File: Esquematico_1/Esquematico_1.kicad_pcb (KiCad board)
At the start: 2 copper layers, 84.5 x 148.5 mm, 83 parts, among them IC1 AP2112K-3.3TRG1, J7 USB_C_Receptacle_USB2.0_16P, U1 ICM-42688-P, U2 STM32F405RGTx, U3 Mag, U4 BMP388, U5 USBLC6-2SC6, U6 TPS54302DDCR

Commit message: Update PCB y JST
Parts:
- removed the XTAL1 at (109.9, 30.8)
- added H1: MountingHole, MountingHole:MountingHole_2.7mm_M2.5_Pad_Via, F.Cu at (88.1, 170.1)
- added H2: MountingHole, MountingHole:MountingHole_2.7mm_M2.5_Pad_Via, F.Cu at (88.1, 136.1)
- added H3: MountingHole, MountingHole:MountingHole_2.7mm_M2.5_Pad_Via, F.Cu at (54.0, 136.0)
- added H4: MountingHole, MountingHole:MountingHole_2.7mm_M2.5_Pad_Via, F.Cu at (53.9, 170.1)
- added J1: Screw_Terminal_01x04, Connector_JST:JST_SH_SM04B-SRSS-TB_1x04-1MP_P1.00mm_Horizontal, F.Cu at (129.0, 144.5)
- added J2: Screw_Terminal_01x03, Connector_JST:JST_SH_SM03B-SRSS-TB_1x03-1MP_P1.00mm_Horizontal, F.Cu at (129.0, 152.0)
- added J3: Screw_Terminal_01x06, Connector_JST:JST_SH_SM06B-SRSS-TB_1x06-1MP_P1.00mm_Horizontal, F.Cu at (128.5, 160.5)
- added J4: Screw_Terminal_01x08, Connector_JST:JST_SH_SM08B-SRSS-TB_1x08-1MP_P1.00mm_Horizontal, F.Cu at (121.0, 168.0)
- added J5: SWD, Connector_PinHeader_1.00mm:PinHeader_1x06_P1.00mm_Vertical_SMD_Pin1Left, F.Cu at (77.6, 78.5)
- moved CARD1 123.5 mm to (64.2, 164.7)
- moved U2 117.1 mm to (113.5, 152.5)
- moved U4 115.4 mm to (81.2, 169.8), turned to 0 degrees
- moved U1 114.1 mm to (77.6, 169.5), turned to 0 degrees
- moved LSE1 109.3 mm to (101.3, 146.5)
- moved C15 108.7 mm to (68.0, 138.0), turned to 180 degrees
- moved L1 107.3 mm to (74.3, 137.0)
- moved C16 106.4 mm to (80.5, 134.5)
- moved R10 106.2 mm to (59.5, 134.5)
- moved R9 106.2 mm to (64.0, 134.5)
- moved C17 105.8 mm to (81.0, 137.0)
- moved C12 104.7 mm to (75.5, 144.1)
- moved R12 104.7 mm to (80.5, 144.5)
- moved R13 104.7 mm to (80.5, 147.4)
- moved C14 104.3 mm to (63.5, 138.5), turned to 90 degrees
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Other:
- board size 84.5 x 148.5 mm -> 84.5 x 148 mm

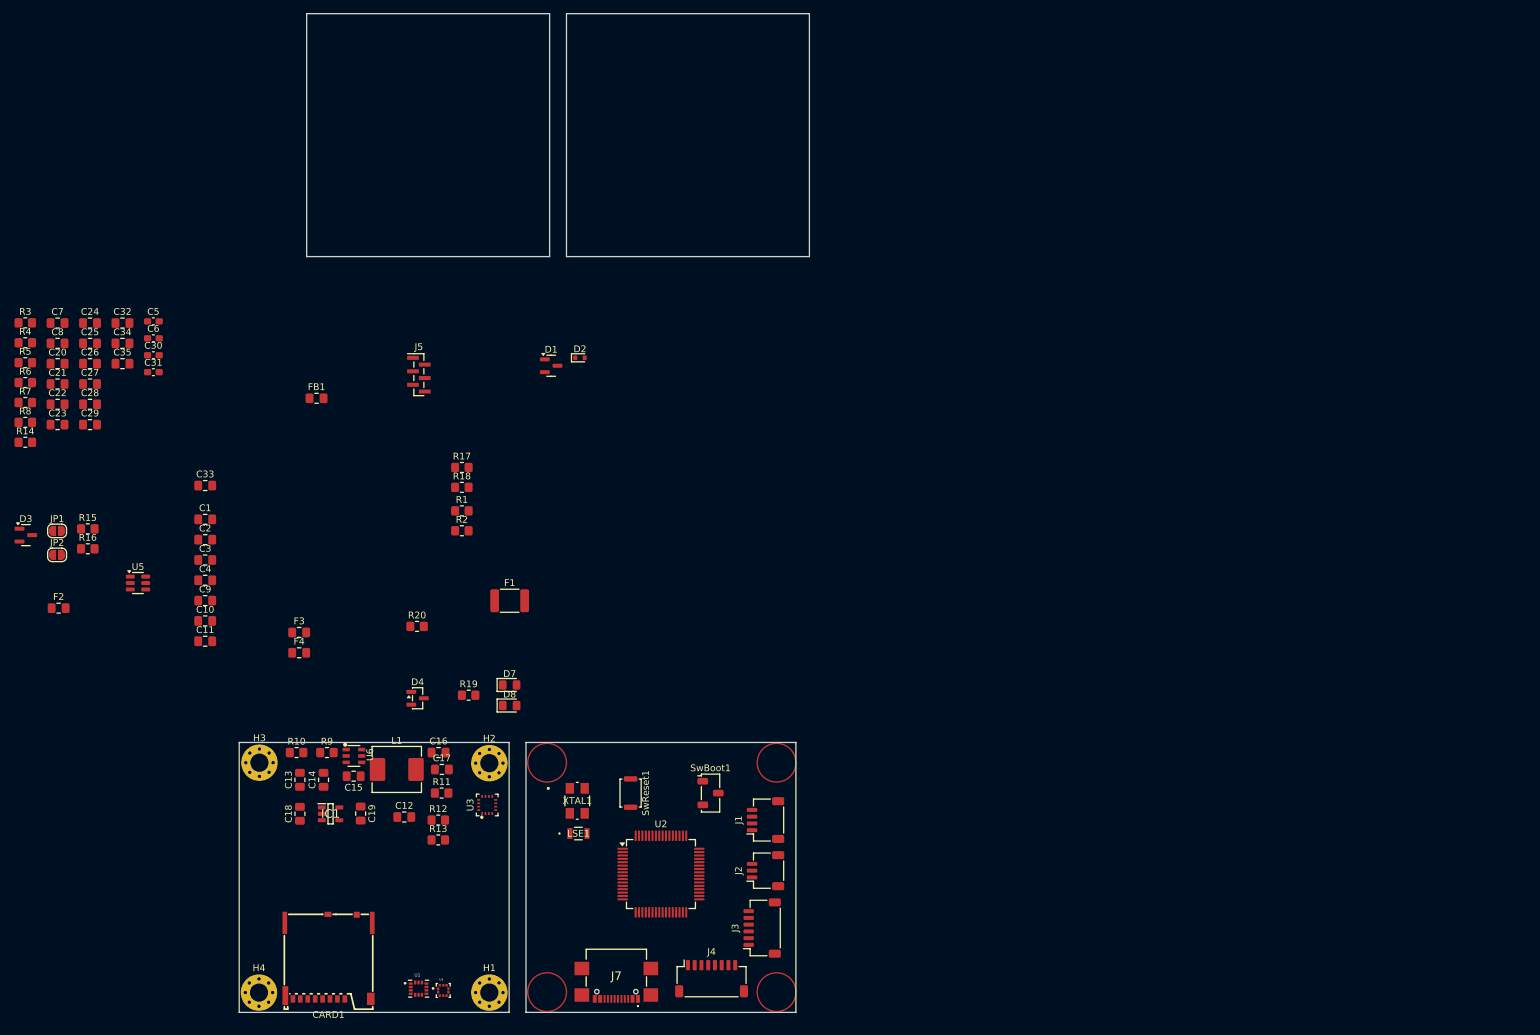
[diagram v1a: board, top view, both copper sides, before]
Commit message: Cambios netclasses, rules en el PCB, conección de los cristales
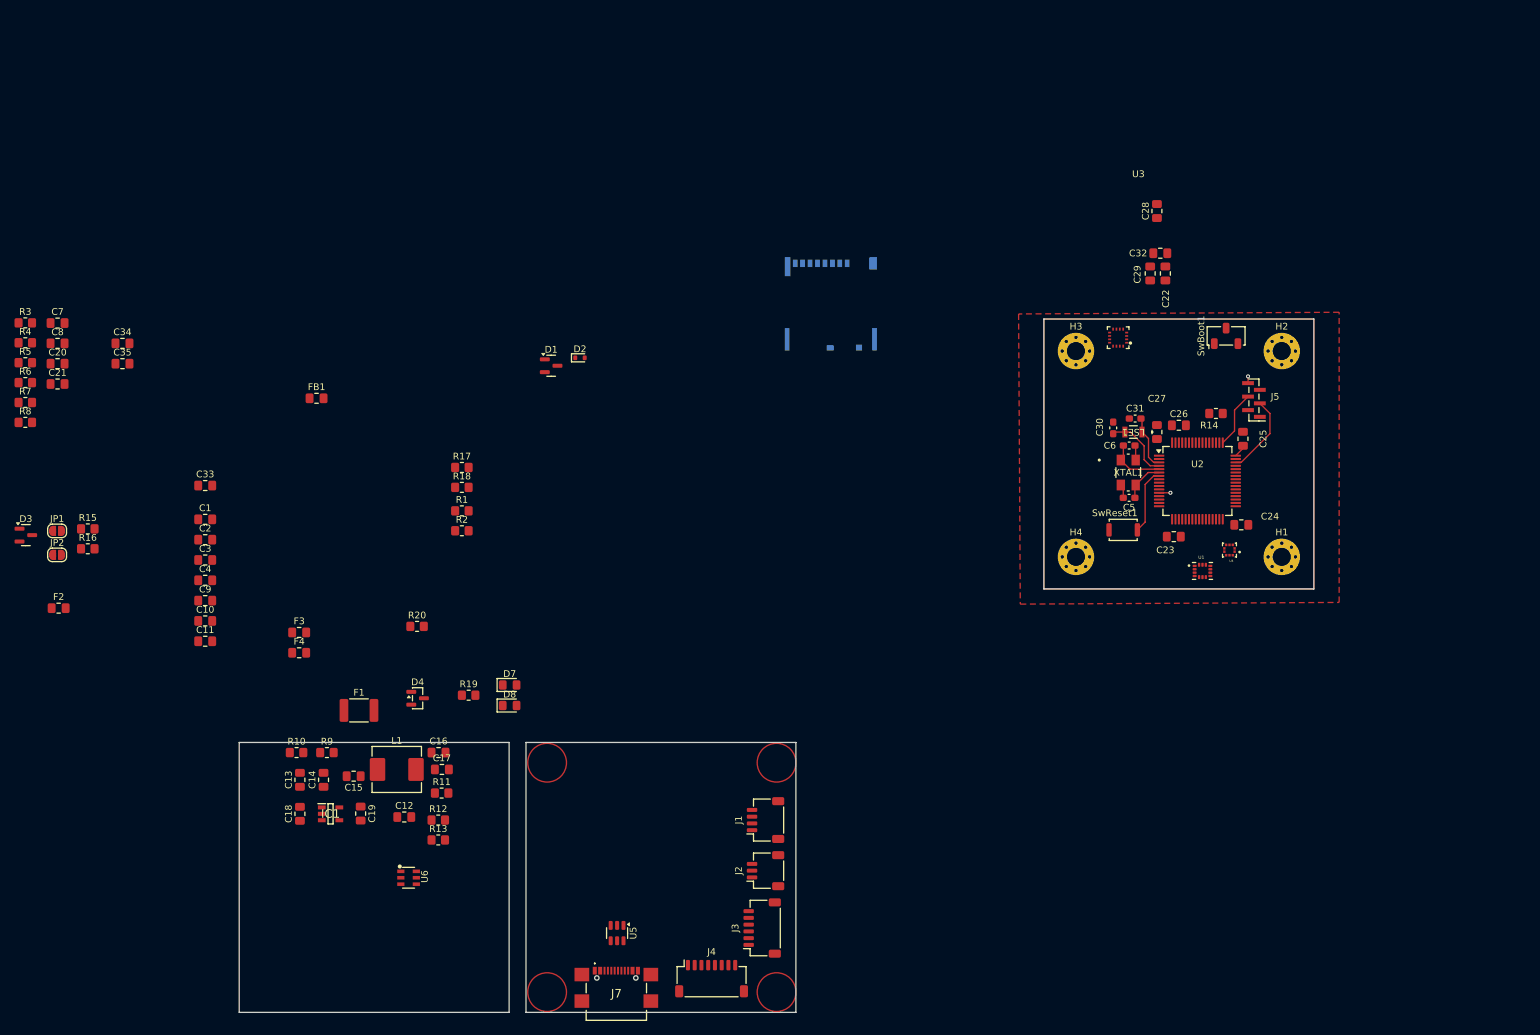
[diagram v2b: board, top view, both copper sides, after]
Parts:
- CARD1: moved to B.Cu
- moved R14 176.5 mm to (195.8, 84.2), turned to 180 degrees
- moved C24 173.2 mm to (199.5, 100.8)
- moved C25 171.4 mm to (199.8, 88.0), turned to 90 degrees
- moved C23 166.2 mm to (189.5, 102.5), turned to 180 degrees
- moved C22 165.3 mm to (188.2, 63.5), turned to 90 degrees
- moved C26 161.6 mm to (190.2, 86.0)
- moved C28 160.7 mm to (187.0, 54.2), turned to 90 degrees
- moved C29 158.7 mm to (186.0, 63.5), turned to 90 degrees
- moved C27 158.3 mm to (187.0, 87.0), turned to 90 degrees
- moved C32 154.1 mm to (187.5, 60.5), turned to 180 degrees
- moved C5 146.9 mm to (182.9, 96.8), turned to 180 degrees
- moved C31 145.6 mm to (183.8, 85.0), turned to 180 degrees
- moved C6 145.5 mm to (182.9, 89.0)
- moved C30 142.6 mm to (180.5, 86.4), turned to 90 degrees
- moved H4 137.2 mm to (175.0, 105.5)
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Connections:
- net SCK_BM renamed CLK_BM
- C16 pad 2: Net-(C16-Pad2) -> LDO_USB
- C17 pad 2: Net-(C16-Pad2) -> LDO_USB
- F1 pad 2: Net-(C16-Pad2) -> LDO_USB
- L1 pad 2: Net-(C16-Pad2) -> LDO_USB
- R11 pad 1: Net-(C16-Pad2) -> LDO_USB
- U2 pad 44: USB_D- -> USB_D+
- U5 pad 6: USB_D- -> USB_D+
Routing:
- net SWDIO: track 0.00 -> 11.9 mm
- net /MCU/LSE_OUT: track 0.00 -> 10.2 mm
- net SWD_NRST: track 0.00 -> 9.81 mm
- net /MCU/HSE_IN: track 0.00 -> 8.54 mm
- net SWCLK: track 0.00 -> 8.38 mm
- net /MCU/LSE_IN: track 0.00 -> 8.09 mm
- net GND: track 0.00 -> 6.92 mm, vias 0 -> 2
- net /MCU/HSE_OUT: track 0.00 -> 6.19 mm
- net +3V3: track 0.00 -> 1.91 mm
- added copper zone on F.Cu, net GND
- added copper zone on In1.Cu, net GND
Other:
- board size 84.5 x 148 mm -> 159.2 x 102.8 mm
- copper layers 2 -> 6

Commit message: Actualizacion
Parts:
- moved C22 42.1 mm to (163.5, 97.5), turned to -90 degrees
- moved C28 29.9 mm to (190.2, 84.0), turned to 0 degrees
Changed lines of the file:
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@@
 		(tags "capacitor handsolder")
 		(property "Reference" "C26"
-			(at 0 -1.68 0)
+			(at -1 -7 0)
 			(layer "F.SilkS")
 			(effects
@@
 		)
 		(property "Value" "100n"
-			(at -0.25 -3 0)
+			(at -1.25 -8.32 0)
 			(layer "F.Fab")
 			(effects
@@
 	(footprint "Capacitor_SMD:C_0805_2012Metric_Pad1.18x1.45mm_HandSolder"
 		(layer "F.Cu")
-		(at 187 54.25 90)
+		(at 190.25 84)
 		(descr "Capacitor SMD 0805 (2012 Metric), square (rectangular) end terminal, IPC-7351 nominal with elongated pad for handsoldering. (Body size source: IPC-SM-782 page 76, https://www.pcb-3d.com/wordpress/wp-content/uploads/ipc-sm-782a_amendment_1_and_2.pdf, https://docs.google.com/spreadsheets/d/1BsfQQcO9C6DZCsRaXUlFlo91Tg2WpOkGARC1WS5S8t0/edit?usp=sharing), generated with kicad-footprint-generator")
 		(tags "capacitor handsolder")
 		(property "Reference" "C28"
-			(at 0 -1.68 90)
+			(at 0 -1.68 0)
 			(layer "F.SilkS")
 			(effects
@@
 		)
 		(property "Value" "4.7u"
-			(at 3.75 0 90)
+			(at 0.25 -3 0)
 			(layer "F.Fab")
 			(effects
@@
 		)
 		(property "Datasheet" "~"
-			(at 0 0 90)
+			(at 0 0 0)
 			(layer "F.Fab")
 			(hide yes)
@@
 		)
 		(property "Description" "Polarized capacitor"
-			(at 0 0 90)
+			(at 0 0 0)
 			(layer "F.Fab")
 			(hide yes)
@@
 		)
 		(fp_line
-			(start 1.88 -0.98)
-			(end 1.88 0.98)
+			(start -1.88 -0.98)
+			(end 1.88 -0.98)
 			(stroke
 				(width 0.05)
@@
 		)
 		(fp_line
-			(start -1.88 -0.98)
-			(end 1.88 -0.98)
+			(start -1.88 0.98)
+			(end -1.88 -0.98)
 			(stroke
 				(width 0.05)
@@
 		)
 		(fp_line
-			(start 1.88 0.98)
-			(end -1.88 0.98)
+			(start 1.88 -0.98)
+			(end 1.88 0.98)
 			(stroke
 				(width 0.05)
@@
 		)
 		(fp_line
-			(start -1.88 0.98)
-			(end -1.88 -0.98)
+			(start 1.88 0.98)
+			(end -1.88 0.98)
 			(stroke
 				(width 0.05)
@@
 		)
 		(fp_line
-			(start 1 -0.625)
-			(end 1 0.625)
+			(start -1 -0.625)
+			(end 1 -0.625)
 			(stroke
 				(width 0.1)
@@
 		)
 		(fp_line
-			(start -1 -0.625)
-			(end 1 -0.625)
+			(start -1 0.625)
+			(end -1 -0.625)
 			(stroke
 				(width 0.1)
@@
 		)
 		(fp_line
-			(start 1 0.625)
-			(end -1 0.625)
+			(start 1 -0.625)
+			(end 1 0.625)
 			(stroke
 				(width 0.1)
@@
 		)
 		(fp_line
-			(start -1 0.625)
-			(end -1 -0.625)
+			(start 1 0.625)
+			(end -1 0.625)
 			(stroke
 				(width 0.1)
@@
 		)
 		(fp_text user "${REFERENCE}"
-			(at 0 0 90)
+			(at 0 0 0)
 			(layer "F.Fab")
 			(effects
@@
 		)
 		(pad "1" smd roundrect
-			(at -1.0375 0 90)
+			(at -1.0375 0)
 			(size 1.175 1.45)
 			(layers "F.Cu" "F.Mask" "F.Paste")
@@
 		)
 		(pad "2" smd roundrect
-			(at 1.0375 0 90)
+			(at 1.0375 0)
 			(size 1.175 1.45)
 			(layers "F.Cu" "F.Mask" "F.Paste")
@@
 	(footprint "Capacitor_SMD:C_0805_2012Metric_Pad1.18x1.45mm_HandSolder"
 		(layer "F.Cu")
-		(at 188.25 63.5 90)
+		(at 163.5 97.5 -90)
 		(descr "Capacitor SMD 0805 (2012 Metric), square (rectangular) end terminal, IPC-7351 nominal with elongated pad for handsoldering. (Body size source: IPC-SM-782 page 76, https://www.pcb-3d.com/wordpress/wp-content/uploads/ipc-sm-782a_amendment_1_and_2.pdf, https://docs.google.com/spreadsheets/d/1BsfQQcO9C6DZCsRaXUlFlo91Tg2WpOkGARC1WS5S8t0/edit?usp=sharing), generated with kicad-footprint-generator")
 		(tags "capacitor handsolder")
@@
 		(attr smd)
 		(fp_line
-			(start -0.261252 -0.735)
-			(end 0.261252 -0.735)
+			(start -0.261252 0.735)
+			(end 0.261252 0.735)
 			(stroke
 				(width 0.12)
@@
 		)
 		(fp_line
-			(start -0.261252 0.735)
-			(end 0.261252 0.735)
+			(start -0.261252 -0.735)
+			(end 0.261252 -0.735)
 			(stroke
 				(width 0.12)
@@
 		)
 		(fp_line
-			(start 1.88 -0.98)
-			(end 1.88 0.98)
+			(start -1.88 0.98)
+			(end -1.88 -0.98)
 			(stroke
 				(width 0.05)
@@
 		)
 		(fp_line
-			(start -1.88 -0.98)
-			(end 1.88 -0.98)
+			(start 1.88 0.98)
+			(end -1.88 0.98)
 			(stroke
 				(width 0.05)
@@
 		)
 		(fp_line
-			(start 1.88 0.98)
-			(end -1.88 0.98)
+			(start -1.88 -0.98)
+			(end 1.88 -0.98)
 			(stroke
 				(width 0.05)
@@
 		)
 		(fp_line
-			(start -1.88 0.98)
-			(end -1.88 -0.98)
+			(start 1.88 -0.98)
+			(end 1.88 0.98)
 			(stroke
 				(width 0.05)
@@
 		)
 		(fp_line
-			(start 1 -0.625)
-			(end 1 0.625)
+			(start -1 0.625)
+			(end -1 -0.625)
 			(stroke
 				(width 0.1)
@@
 		)
 		(fp_line
-			(start -1 -0.625)
-			(end 1 -0.625)
+			(start 1 0.625)
+			(end -1 0.625)
 			(stroke
 				(width 0.1)
@@
 		)
 		(fp_line
-			(start 1 0.625)
-			(end -1 0.625)
+			(start -1 -0.625)
+			(end 1 -0.625)
 			(stroke
 				(width 0.1)
@@
 		)
 		(fp_line
-			(start -1 0.625)
-			(end -1 -0.625)
+			(start 1 -0.625)
+			(end 1 0.625)
 			(stroke
 				(width 0.1)
@@
 		)
 		(pad "1" smd roundrect
-			(at -1.0375 0 90)
+			(at -1.0375 0 270)
 			(size 1.175 1.45)
 			(layers "F.Cu" "F.Mask" "F.Paste")
@@
 		)
 		(pad "2" smd roundrect
-			(at 1.0375 0 90)
+			(at 1.0375 0 270)
 			(size 1.175 1.45)
 			(layers "F.Cu" "F.Mask" "F.Paste")
@@
 		(tags "capacitor handsolder")
 		(property "Reference" "C27"
-			(at 4.9625 0 0)
+			(at 6.5 -2.75 0)
 			(layer "F.SilkS")
 			(effects
@@
 		)
 		(property "Value" "100n"
-			(at 3.7125 -0.25 180)
+			(at 5.25 -3 180)
 			(layer "F.Fab")
 			(effects
@@
 			)
 		)
+	)
+	(zone
+		(net 0)
+		(net_name "")
+		(layer "F.Cu")
+		(hatch edge 0.5)
+		(connect_pads
+			(clearance 0)
+		)
+		(min_thickness 0.25)
+		(filled_areas_thickness no)
+		(keepout
+			(tracks not_allowed)
+			(vias not_allowed)
+			(pads not_allowed)
+			(copperpour not_allowed)
+			(footprints allowed)
+		)
+		(placement
+			(enabled no)
+			(sheetname "/")
+		)
+		(fill
+			(thermal_gap 0.5)
+			(thermal_bridge_width 0.5)
+		)
+		(polygon
+			(pts
+				(xy 195.5 109.1) (xy 195.5 106.1) (xy 192 106.1) (xy 192 109.1)
+			)
+		)

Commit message: BIG Update conexionado MCU y PCB
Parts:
- added F5: 750mA, Capacitor_SMD:C_0805_2012Metric_Pad1.18x1.45mm_HandSolder, F.Cu at (96.8, 133.3)
- added J6: Screw_Terminal_01x04, Connector_JST:JST_SH_SM04B-SRSS-TB_1x04-1MP_P1.00mm_Horizontal, F.Cu at (98.8, 128.0)
- H1, H2, H3, H4: footprint MountingHole:MountingHole_2.7mm_M2.5_Pad_Via -> MountingHole:MountingHole_3.2mm_M3_Pad_Via
- J1, J2, J3, J4, J7, U5: moved to B.Cu
- moved C7 185.6 mm to (209.2, 57.4)
- moved C8 185.6 mm to (209.2, 60.4)
- moved C20 183.1 mm to (201.9, 120.6)
- moved C21 183.1 mm to (201.9, 123.6)
- moved C10 181.6 mm to (226.8, 97.9)
- moved C11 181.6 mm to (226.8, 100.9)
- moved C9 181.5 mm to (226.7, 95.5)
- moved C1 179.3 mm to (223.2, 72.8)
- moved C4 179.3 mm to (223.2, 81.9)
- moved C2 173.9 mm to (219.3, 116.5)
- moved C3 173.9 mm to (219.3, 119.5)
- moved FB1 155.3 mm to (216.1, 59.4)
- moved R1 143.0 mm to (226.6, 108.5)
- moved R2 143.0 mm to (226.6, 111.5)
- moved R19 122.8 mm to (206.7, 142.1)
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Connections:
- U2 pad 10: MISO_BM -> INT1_IMU
- U2 pad 11: MOSI_BM -> INT2_IMU
- U2 pad 16: unconnected-(U2-PA2-Pad16) -> ESC3
- U2 pad 17: unconnected-(U2-PA3-Pad17) -> ESC4
- U2 pad 20: AP_CS_IMU -> unconnected-(U2-PA4-Pad20)
- U2 pad 24: unconnected-(U2-PC4-Pad24) -> CRT
- U2 pad 25: unconnected-(U2-PC5-Pad25) -> AP_CS_IMU
- U2 pad 26: CS_BM -> unconnected-(U2-PB0-Pad26)
- U2 pad 29: CLK_BM -> GPS_UART_TX
- U2 pad 30: unconnected-(U2-PB11-Pad30) -> GPS_UART_RX
- U2 pad 33: unconnected-(U2-PB12-Pad33) -> CS_BM
- U2 pad 34: unconnected-(U2-PB13-Pad34) -> CLK_BM
- U2 pad 35: unconnected-(U2-PB14-Pad35) -> MISO_BM
- U2 pad 36: unconnected-(U2-PB15-Pad36) -> MOSI_BM
- U2 pad 38: unconnected-(U2-PC7-Pad38) -> TELEM_ESC
- U2 pad 44: USB_D+ -> USB_D-
- U2 pad 50: unconnected-(U2-PA15-Pad50) -> ESC1
- U2 pad 55: unconnected-(U2-PB3-Pad55) -> ESC2
- U2 pad 56: unconnected-(U2-PB4-Pad56) -> CardDetect
- U2 pad 9: unconnected-(U2-PC1-Pad9) -> INT_BM
- U5 pad 6: USB_D+ -> USB_D-
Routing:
- net CLK_IMU: track 0.00 -> 2.08 mm
- net MISO_IMU: track 0.00 -> 1.87 mm
- added copper zone on B.Cu, net GND
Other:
- board size 159.2 x 102.8 mm -> 116.8 x 46.1 mm
- board text added: "HERNAN"
- board text added: "LUCAS"

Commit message: Push prueba PCB LUCAS
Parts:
- C12, C13, C14, C15, C16, C17, C18, C19, C33, C34, C35, D1, D2, D3, D4, F1, F2, F3, F4, F5, IC1, J6, JP1, JP2, L1, R10, R11, R12, R13, R15, R16, R17, R18, R3, R4, R5, R6, R7, R8, R9, U6: moved to B.Cu
- moved F3 75.3 mm to (134.9, 123.2), turned to 180 degrees
- moved F4 75.3 mm to (134.9, 126.2), turned to 180 degrees
- moved R10 75.0 mm to (134.5, 134.3), turned to 180 degrees
- moved C13 74.0 mm to (134.0, 138.3)
- moved C18 74.0 mm to (134.0, 143.4)
- moved R17 72.9 mm to (96.0, 150.4), turned to 180 degrees
- moved R18 72.9 mm to (96.0, 153.4), turned to 180 degrees
- moved D3 71.9 mm to (83.6, 134.5), turned to 180 degrees
- moved C14 67.0 mm to (130.5, 138.3)
- moved R9 66.0 mm to (130.0, 134.3), turned to 180 degrees
- moved IC1 64.9 mm to (129.4, 143.4), turned to 180 degrees
- moved D1 64.7 mm to (99.6, 143.7), turned to 180 degrees
- moved JP2 63.7 mm to (79.0, 137.4), turned to 180 degrees
- moved JP1 63.7 mm to (79.0, 133.8), turned to 180 degrees
- moved F2 63.3 mm to (78.8, 145.3), turned to 180 degrees
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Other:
- board text added: "F: HIGH SPEED SIGNAL + GND IN1: GND IN2: LOW SPEED SIGNAL IN3: CAPA POTENCIA IN4: GND B: HIGH SPEED SIGNAL + GND"

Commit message: Update PCB
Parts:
- added H4: MountingHole, MountingHole:MountingHole_3.2mm_M3_Pad_Via, B.Cu at (103.0, 86.1)
- added H4: MountingHole, MountingHole:MountingHole_3.2mm_M3_Pad_Via, B.Cu at (123.1, 106.4)
- added H4: MountingHole, MountingHole:MountingHole_3.2mm_M3_Pad_Via, B.Cu at (103.0, 106.4)
- added H4: MountingHole, MountingHole:MountingHole_3.2mm_M3_Pad_Via, B.Cu at (123.1, 86.1)
- moved J6 49.6 mm to (114.5, 81.0), turned to 0 degrees
- moved J7 19.3 mm to (131.2, 67.6)
- moved J1 16.4 mm to (114.0, 101.0)
- moved J2 6.67 mm to (97.0, 111.0), turned to 90 degrees
- moved U5 5.07 mm to (121.1, 91.5)
- moved CARD1 3.45 mm to (101.7, 95.2)
- moved J3 3.27 mm to (115.3, 112.0)
- moved J4 0.60 mm to (129.3, 100.0)
- turned U3 to -90 degrees

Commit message: Diodo de mierda
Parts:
- removed the H4 at (103.0, 86.1)
- removed the H4 at (123.1, 106.4)
- removed the H4 at (103.0, 106.4)
- removed the H4 at (123.1, 86.1)
- D2: footprint Diode_SMD:D_SOD-523 -> Diode_SMD:D_SMB_Handsoldering
